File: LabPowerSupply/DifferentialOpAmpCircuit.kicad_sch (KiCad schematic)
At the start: 12 parts

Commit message: almost done
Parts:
- removed R1_OA1: 4k, Resistor_SMD:R_0603_1608Metric, symbol Device:R_US
- added R11_OA1, R12_OA1: 2k, symbol Device:R_US
- added R52_OA2: 2k, Resistor_SMD:R_0603_1608Metric, symbol Device:R_US
- added R92_OA2: 1k, Resistor_SMD:R_0603_1608Metric, symbol Device:R_US
- R51_OA1: renamed from R5_OA1; value 4k -> 2k
- R91_OA1: renamed from R9_OA1; value 3k -> 2k
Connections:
- net 3.3 Volts: now also R11_OA1.1
- net ADC: now also R92_OA2.2; no longer R91_OA1.2
- net at OpAmp1.3 (+), R2_OA1.1: now also R12_OA1.2
- net at OpAmp1.6 (-), R6_OA1.1: now also R52_OA2.2; no longer R51_OA1.2
- new net: R91_OA1.2, R92_OA2.1
- new net: R51_OA1.2, R52_OA2.1
- new net: R11_OA1.2, R12_OA1.1
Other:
- moved on the sheet: OpAmp1D, R10_OA1, R11_OA1, R6_OA1, R8_OA1

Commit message: Update pcb footprints
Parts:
- R12_OA1: footprint (none) -> Resistor_SMD:R_0603_1608Metric
- R13_OA1: renamed from R11_OA1; footprint (none) -> Resistor_SMD:R_0603_1608Metric
- renumbered R52_OA2 to R52_OA1, R92_OA2 to R92_OA1
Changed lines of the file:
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@@
   (symbol (lib_id "Device:R_US") (at 166.37 113.03 0) (unit 1)
     (in_bom yes) (on_board yes) (fields_autoplaced)
-    (property "Reference" "R92_OA2" (id 0) (at 168.91 111.7599 0)
+    (property "Reference" "R92_OA1" (id 0) (at 168.91 111.7599 0)
       (effects (font (size 1.27 1.27)) (justify left))
     )
@@
   (symbol (lib_id "Device:R_US") (at 137.16 115.57 0) (unit 1)
     (in_bom yes) (on_board yes) (fields_autoplaced)
-    (property "Reference" "R52_OA2" (id 0) (at 139.7 114.2999 0)
+    (property "Reference" "R52_OA1" (id 0) (at 139.7 114.2999 0)
       (effects (font (size 1.27 1.27)) (justify left))
     )
@@
     (property "Reference" "R12_OA1" (id 0) (at 109.22 77.47 90))
     (property "Value" "2k" (id 1) (at 107.95 80.01 90))
-    (property "Footprint" "" (id 2) (at 108.204 82.804 90)
+    (property "Footprint" "Resistor_SMD:R_0603_1608Metric" (id 2) (at 108.204 82.804 90)
       (effects (font (size 1.27 1.27)) hide)
     )
@@
   (symbol (lib_id "Device:R_US") (at 100.33 83.82 90) (unit 1)
     (in_bom yes) (on_board yes)
-    (property "Reference" "R11_OA1" (id 0) (at 99.06 77.47 90))
+    (property "Reference" "R13_OA1" (id 0) (at 99.06 77.47 90))
     (property "Value" "2k" (id 1) (at 100.33 80.01 90))
-    (property "Footprint" "" (id 2) (at 100.584 82.804 90)
-      (effects (font (size 1.27 1.27)) hide)
-    )
+    (property "Footprint" "Resistor_SMD:R_0603_1608Metric" (id 2) (at 100.584 82.804 90)
+      (effects (font (size 1.27 1.27)) hide)
+    )

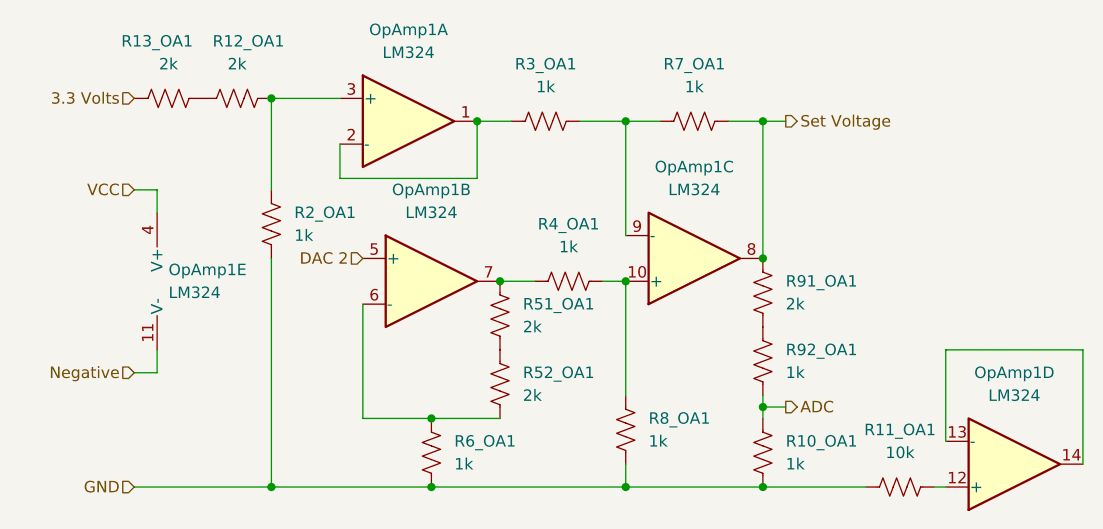
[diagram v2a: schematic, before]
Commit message: Updated Part List
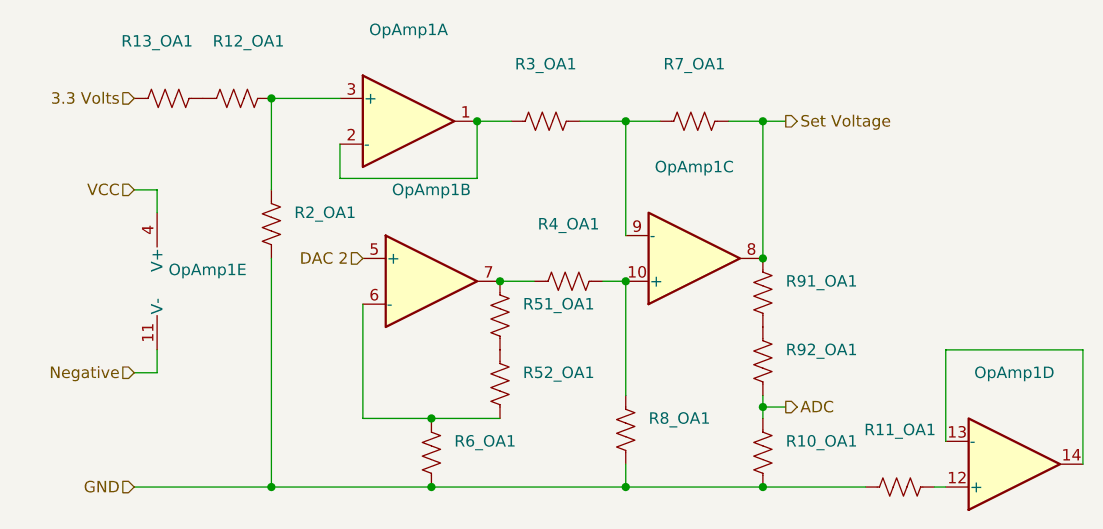
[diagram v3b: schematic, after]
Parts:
- OpAmp1: value LM324 -> (none); footprint Package_SO:SOIC-14_3.9x8.7mm_P1.27mm -> (none)
- R10_OA1, R2_OA1, R3_OA1, R4_OA1, R6_OA1, R7_OA1, R8_OA1, R92_OA1: value 1k -> (none); footprint Resistor_SMD:R_0603_1608Metric -> (none)
- R11_OA1: value 10k -> (none); footprint Resistor_SMD:R_0603_1608Metric -> (none)
- R12_OA1, R13_OA1, R51_OA1, R52_OA1, R91_OA1: value 2k -> (none); footprint Resistor_SMD:R_0603_1608Metric -> (none)
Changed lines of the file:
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@@
       (effects (font (size 1.27 1.27)) (justify left))
     )
-    (property "Value" "2k" (id 1) (at 168.91 106.6799 0)
-      (effects (font (size 1.27 1.27)) (justify left))
-    )
-    (property "Footprint" "Resistor_SMD:R_0603_1608Metric" (id 2) (at 167.386 105.664 90)
+    (property "Value" "" (id 1) (at 168.91 106.6799 0)
+      (effects (font (size 1.27 1.27)) (justify left))
+    )
+    (property "Footprint" "" (id 2) (at 167.386 105.664 90)
       (effects (font (size 1.27 1.27)) hide)
     )
@@
       (effects (font (size 1.27 1.27)) (justify left))
     )
-    (property "Value" "1k" (id 1) (at 168.91 114.2999 0)
-      (effects (font (size 1.27 1.27)) (justify left))
-    )
-    (property "Footprint" "Resistor_SMD:R_0603_1608Metric" (id 2) (at 167.386 113.284 90)
+    (property "Value" "" (id 1) (at 168.91 114.2999 0)
+      (effects (font (size 1.27 1.27)) (justify left))
+    )
+    (property "Footprint" "" (id 2) (at 167.386 113.284 90)
       (effects (font (size 1.27 1.27)) hide)
     )
@@
       (effects (font (size 1.27 1.27)) (justify left))
     )
-    (property "Value" "LM324" (id 1) (at 100.33 105.4099 0)
-      (effects (font (size 1.27 1.27)) (justify left))
-    )
-    (property "Footprint" "Package_SO:SOIC-14_3.9x8.7mm_P1.27mm" (id 2) (at 100.33 101.6 0)
+    (property "Value" "" (id 1) (at 100.33 105.4099 0)
+      (effects (font (size 1.27 1.27)) (justify left))
+    )
+    (property "Footprint" "" (id 2) (at 100.33 101.6 0)
       (effects (font (size 1.27 1.27)) hide)
     )
@@
     (in_bom yes) (on_board yes) (fields_autoplaced)
     (property "Reference" "R3_OA1" (id 0) (at 142.24 80.01 90))
-    (property "Value" "1k" (id 1) (at 142.24 82.55 90))
-    (property "Footprint" "Resistor_SMD:R_0603_1608Metric" (id 2) (at 142.494 85.344 90)
+    (property "Value" "" (id 1) (at 142.24 82.55 90))
+    (property "Footprint" "" (id 2) (at 142.494 85.344 90)
       (effects (font (size 1.27 1.27)) hide)
     )
@@
       (effects (font (size 1.27 1.27)) (justify left))
     )
-    (property "Value" "2k" (id 1) (at 139.7 116.8399 0)
-      (effects (font (size 1.27 1.27)) (justify left))
-    )
-    (property "Footprint" "Resistor_SMD:R_0603_1608Metric" (id 2) (at 138.176 115.824 90)
+    (property "Value" "" (id 1) (at 139.7 116.8399 0)
+      (effects (font (size 1.27 1.27)) (justify left))
+    )
+    (property "Footprint" "" (id 2) (at 138.176 115.824 90)
       (effects (font (size 1.27 1.27)) hide)
     )
@@
     (in_bom yes) (on_board yes)
     (property "Reference" "R12_OA1" (id 0) (at 109.22 77.47 90))
-    (property "Value" "2k" (id 1) (at 107.95 80.01 90))
-    (property "Footprint" "Resistor_SMD:R_0603_1608Metric" (id 2) (at 108.204 82.804 90)
+    (property "Value" "" (id 1) (at 107.95 80.01 90))
+    (property "Footprint" "" (id 2) (at 108.204 82.804 90)
       (effects (font (size 1.27 1.27)) hide)
     )
@@
       (effects (font (size 1.27 1.27)) (justify left))
     )
-    (property "Value" "1k" (id 1) (at 114.3 99.0599 0)
-      (effects (font (size 1.27 1.27)) (justify left))
-    )
-    (property "Footprint" "Resistor_SMD:R_0603_1608Metric" (id 2) (at 112.776 98.044 90)
+    (property "Value" "" (id 1) (at 114.3 99.0599 0)
+      (effects (font (size 1.27 1.27)) (justify left))
+    )
+    (property "Footprint" "" (id 2) (at 112.776 98.044 90)
       (effects (font (size 1.27 1.27)) hide)
     )
@@
       (effects (font (size 1.27 1.27)) (justify left))
     )
-    (property "Value" "1k" (id 1) (at 132.08 124.4599 0)
-      (effects (font (size 1.27 1.27)) (justify left))
-    )
-    (property "Footprint" "Resistor_SMD:R_0603_1608Metric" (id 2) (at 130.556 123.444 90)
+    (property "Value" "" (id 1) (at 132.08 124.4599 0)
+      (effects (font (size 1.27 1.27)) (justify left))
+    )
+    (property "Footprint" "" (id 2) (at 130.556 123.444 90)
       (effects (font (size 1.27 1.27)) hide)
     )
@@
     (in_bom yes) (on_board yes) (fields_autoplaced)
     (property "Reference" "R4_OA1" (id 0) (at 144.78 97.79 90))
-    (property "Value" "1k" (id 1) (at 144.78 100.33 90))
-    (property "Footprint" "Resistor_SMD:R_0603_1608Metric" (id 2) (at 145.034 103.124 90)
+    (property "Value" "" (id 1) (at 144.78 100.33 90))
+    (property "Footprint" "" (id 2) (at 145.034 103.124 90)
       (effects (font (size 1.27 1.27)) hide)
     )
@@
     (in_bom yes) (on_board yes) (fields_autoplaced)
     (property "Reference" "R11_OA1" (id 0) (at 181.61 120.65 90))
-    (property "Value" "10k" (id 1) (at 181.61 123.19 90))
-    (property "Footprint" "Resistor_SMD:R_0603_1608Metric" (id 2) (at 181.864 125.984 90)
+    (property "Value" "" (id 1) (at 181.61 123.19 90))
+    (property "Footprint" "" (id 2) (at 181.864 125.984 90)
       (effects (font (size 1.27 1.27)) hide)
     )
@@
     (in_bom yes) (on_board yes) (fields_autoplaced)
     (property "Reference" "OpAmp1" (id 0) (at 129.54 93.98 0))
-    (property "Value" "LM324" (id 1) (at 129.54 96.52 0))
-    (property "Footprint" "Package_SO:SOIC-14_3.9x8.7mm_P1.27mm" (id 2) (at 128.27 101.6 0)
+    (property "Value" "" (id 1) (at 129.54 96.52 0))
+    (property "Footprint" "" (id 2) (at 128.27 101.6 0)
       (effects (font (size 1.27 1.27)) hide)
     )
@@
     (in_bom yes) (on_board yes) (fields_autoplaced)
     (property "Reference" "OpAmp1" (id 0) (at 127 76.2 0))
-    (property "Value" "LM324" (id 1) (at 127 78.74 0))
-    (property "Footprint" "Package_SO:SOIC-14_3.9x8.7mm_P1.27mm" (id 2) (at 125.73 83.82 0)
+    (property "Value" "" (id 1) (at 127 78.74 0))
+    (property "Footprint" "" (id 2) (at 125.73 83.82 0)
       (effects (font (size 1.27 1.27)) hide)
     )
@@
       (effects (font (size 1.27 1.27)) (justify left))
     )
-    (property "Value" "1k" (id 1) (at 168.91 124.4599 0)
-      (effects (font (size 1.27 1.27)) (justify left))
-    )
-    (property "Footprint" "Resistor_SMD:R_0603_1608Metric" (id 2) (at 167.386 123.444 90)
+    (property "Value" "" (id 1) (at 168.91 124.4599 0)
+      (effects (font (size 1.27 1.27)) (justify left))
+    )
+    (property "Footprint" "" (id 2) (at 167.386 123.444 90)
       (effects (font (size 1.27 1.27)) hide)
     )
@@
     (in_bom yes) (on_board yes) (fields_autoplaced)
     (property "Reference" "R7_OA1" (id 0) (at 158.75 80.01 90))
-    (property "Value" "1k" (id 1) (at 158.75 82.55 90))
-    (property "Footprint" "Resistor_SMD:R_0603_1608Metric" (id 2) (at 159.004 85.344 90)
+    (property "Value" "" (id 1) (at 158.75 82.55 90))
+    (property "Footprint" "" (id 2) (at 159.004 85.344 90)
       (effects (font (size 1.27 1.27)) hide)
     )
@@
     (in_bom yes) (on_board yes) (fields_autoplaced)
     (property "Reference" "OpAmp1" (id 0) (at 194.31 114.3 0))
-    (property "Value" "LM324" (id 1) (at 194.31 116.84 0))
-    (property "Footprint" "Package_SO:SOIC-14_3.9x8.7mm_P1.27mm" (id 2) (at 193.04 127 0)
+    (property "Value" "" (id 1) (at 194.31 116.84 0))
+    (property "Footprint" "" (id 2) (at 193.04 127 0)
       (effects (font (size 1.27 1.27)) hide)
     )
@@
       (effects (font (size 1.27 1.27)) (justify left))
     )
-    (property "Value" "1k" (id 1) (at 153.67 121.9199 0)
-      (effects (font (size 1.27 1.27)) (justify left))
-    )
-    (property "Footprint" "Resistor_SMD:R_0603_1608Metric" (id 2) (at 152.146 120.904 90)
+    (property "Value" "" (id 1) (at 153.67 121.9199 0)
+      (effects (font (size 1.27 1.27)) (justify left))
+    )
+    (property "Footprint" "" (id 2) (at 152.146 120.904 90)
       (effects (font (size 1.27 1.27)) hide)
     )
@@
       (effects (font (size 1.27 1.27)) (justify left))
     )
-    (property "Value" "2k" (id 1) (at 139.7 109.2199 0)
-      (effects (font (size 1.27 1.27)) (justify left))
-    )
-    (property "Footprint" "Resistor_SMD:R_0603_1608Metric" (id 2) (at 138.176 108.204 90)
+    (property "Value" "" (id 1) (at 139.7 109.2199 0)
+      (effects (font (size 1.27 1.27)) (justify left))
+    )
+    (property "Footprint" "" (id 2) (at 138.176 108.204 90)
       (effects (font (size 1.27 1.27)) hide)
     )
@@
     (in_bom yes) (on_board yes)
     (property "Reference" "R13_OA1" (id 0) (at 99.06 77.47 90))
-    (property "Value" "2k" (id 1) (at 100.33 80.01 90))
-    (property "Footprint" "Resistor_SMD:R_0603_1608Metric" (id 2) (at 100.584 82.804 90)
+    (property "Value" "" (id 1) (at 100.33 80.01 90))
+    (property "Footprint" "" (id 2) (at 100.584 82.804 90)
       (effects (font (size 1.27 1.27)) hide)
     )
@@
     (in_bom yes) (on_board yes) (fields_autoplaced)
     (property "Reference" "OpAmp1" (id 0) (at 158.75 91.44 0))
-    (property "Value" "LM324" (id 1) (at 158.75 93.98 0))
-    (property "Footprint" "Package_SO:SOIC-14_3.9x8.7mm_P1.27mm" (id 2) (at 157.48 104.14 0)
-      (effects (font (size 1.27 1.27)) hide)
-    )
+    (property "Value" "" (id 1) (at 158.75 93.98 0))
+    (property "Footprint" "" (id 2) (at 157.48 104.14 0)
+      (effects (font (size 1.27 1.27)) hide)
+    )
